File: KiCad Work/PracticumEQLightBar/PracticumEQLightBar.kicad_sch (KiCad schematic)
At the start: 2 parts, among them U1 TEENSY 4.1, U2 TEENSY AUDIO ADAPTER BOARD RE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

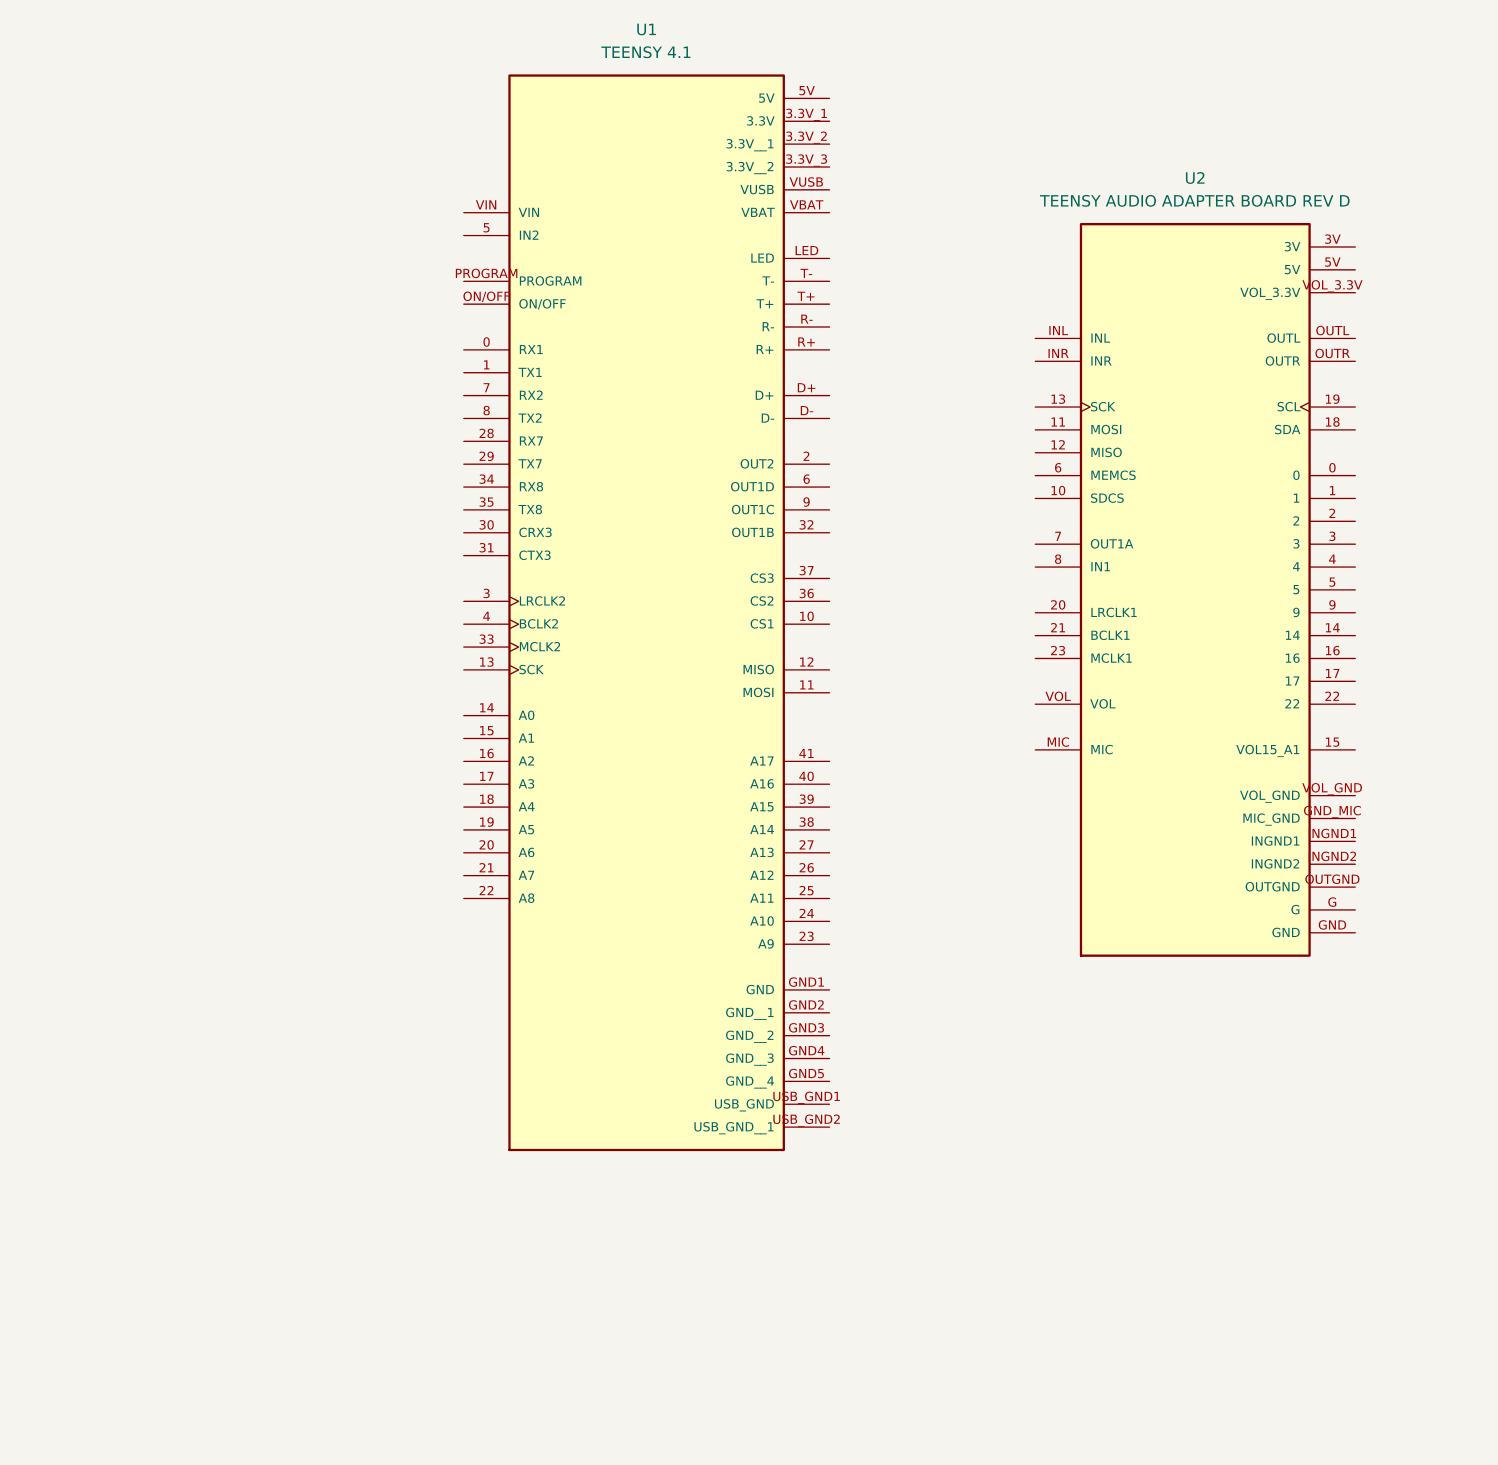
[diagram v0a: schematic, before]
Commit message: Added LEDs and wired them in schematic
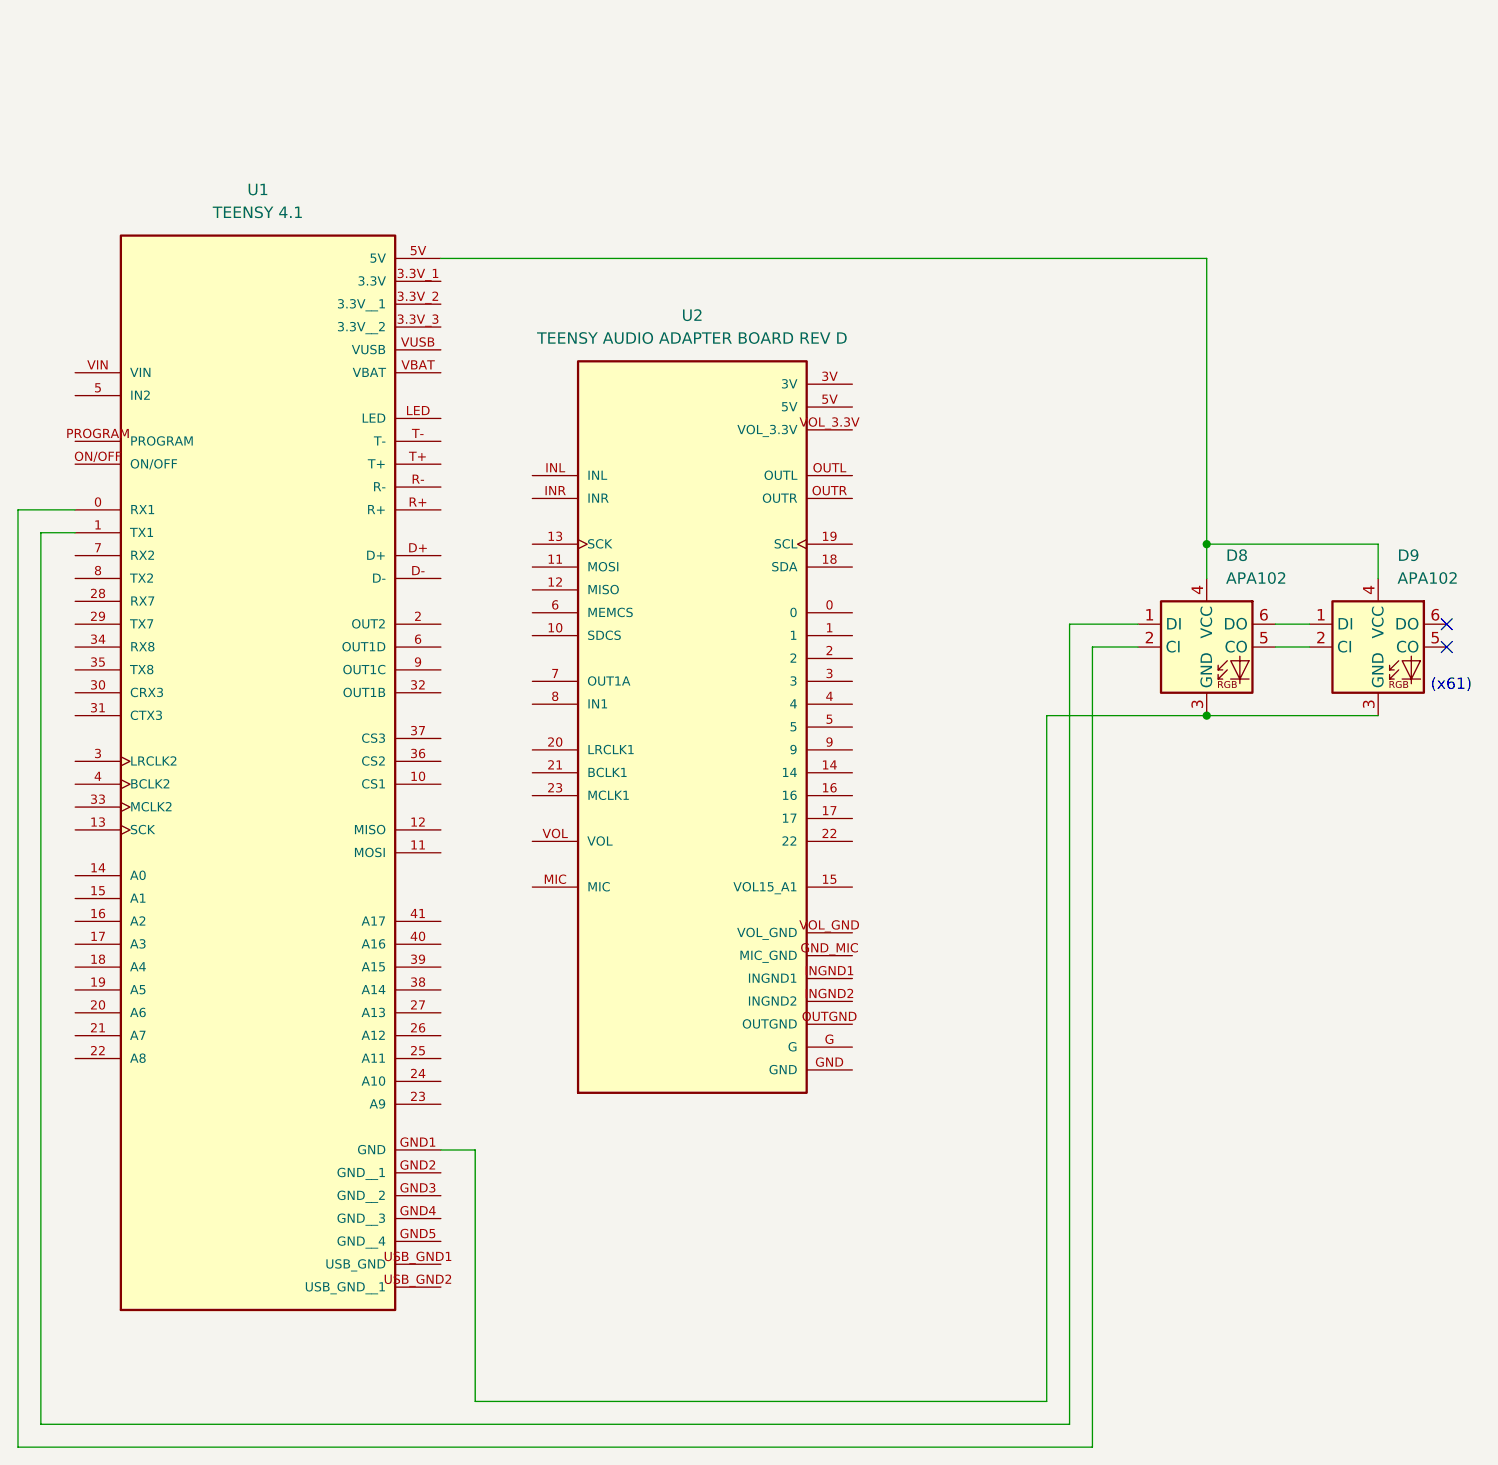
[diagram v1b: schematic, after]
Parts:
- added D8, D9: APA102, LED_SMD:LED_RGB_5050-6, symbol LED:APA102
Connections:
- net at U1.0 (RX1): now also D8.2 (CI)
- net at U1.1 (TX1): now also D8.1 (DI)
- net at U1.5V: now also D8.4 (VCC), D9.4 (VCC)
- net at U1.GND1 (GND): now also D8.3 (GND), D9.3 (GND)
- new net: D8.5 (CO), D9.2 (CI)
- new net: D8.6 (DO), D9.1 (DI)
- no-connect marks 0 -> 2
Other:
- note added: "(x61)"
- moved on the sheet: U1, U2

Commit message: Updates to LED layout to match 49 key on schematic and PCB
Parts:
- added D1, D10, D11, D12, D13, D14, D15, D16, D17, D18, D19, D2, D20, D21, D22, D23, D24, D25, D26, D27, D28, D29, D3, D30, D31, D32, D33, D34, D35, D36, D37, D38, D39, D4, D40, D41, D42, D43, D44, D45, D46, D47, D48, D49, D5, D6, D7: APA102, LED_SMD:LED_RGB_5050-6, symbol LED:APA102
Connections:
- net at U1.0 (RX1): now also D1.2 (CI); no longer D8.2 (CI)
- net at U1.1 (TX1): now also D1.1 (DI); no longer D8.1 (DI)
- net at D8.4 (VCC), D9.4 (VCC), U1.5V: now also D1.4 (VCC), D10.4 (VCC), D11.4 (VCC), D12.4 (VCC), D13.4 (VCC), D14.4 (VCC), D15.4 (VCC), D16.4 (VCC), D17.4 (VCC), D18.4 (VCC), D19.4 (VCC), D2.4 (VCC), D20.4 (VCC), D21.4 (VCC), D22.4 (VCC), D23.4 (VCC), D24.4 (VCC), D25.4 (VCC), D26.4 (VCC), D27.4 (VCC), D28.4 (VCC), D29.4 (VCC), D3.4 (VCC), D30.4 (VCC), D31.4 (VCC), D32.4 (VCC), D33.4 (VCC), D34.4 (VCC), D35.4 (VCC), D36.4 (VCC), D37.4 (VCC), D38.4 (VCC), D39.4 (VCC), D4.4 (VCC), D40.4 (VCC), D41.4 (VCC), D42.4 (VCC), D43.4 (VCC), D44.4 (VCC), D45.4 (VCC), D46.4 (VCC), D47.4 (VCC), D48.4 (VCC), D49.4 (VCC), D5.4 (VCC), D6.4 (VCC), D7.4 (VCC)
- net GND: now reaches D8.3 (GND), D9.3 (GND)
- net GND: now also D1.3 (GND), D10.3 (GND), D11.3 (GND), D12.3 (GND), D13.3 (GND), D14.3 (GND), D15.3 (GND), D16.3 (GND), D17.3 (GND), D18.3 (GND), D19.3 (GND), D2.3 (GND), D20.3 (GND), D21.3 (GND), D22.3 (GND), D23.3 (GND), D24.3 (GND), D25.3 (GND), D26.3 (GND), D27.3 (GND), D28.3 (GND), D29.3 (GND), D3.3 (GND), D30.3 (GND), D31.3 (GND), D32.3 (GND), D33.3 (GND), D34.3 (GND), D35.3 (GND), D36.3 (GND), D37.3 (GND), D38.3 (GND), D39.3 (GND), D4.3 (GND), D40.3 (GND), D41.3 (GND), D42.3 (GND), D43.3 (GND), D44.3 (GND), D45.3 (GND), D46.3 (GND), D47.3 (GND), D48.3 (GND), D49.3 (GND), D5.3 (GND), D6.3 (GND), D7.3 (GND); no longer U1.GND1 (GND)
- net at D9.5 (CO): now also D10.2 (CI)
- net at D9.6 (DO): now also D10.1 (DI)
- new net: D18.6 (DO), D19.1 (DI)
- new net: D18.5 (CO), D19.2 (CI)
- new net: D19.5 (CO), D20.2 (CI)
- new net: D19.6 (DO), D20.1 (DI)
- new net: D36.6 (DO), D37.1 (DI)
- new net: D36.5 (CO), D37.2 (CI)
- new net: D37.5 (CO), D38.2 (CI)
- new net: D37.6 (DO), D38.1 (DI)
- new net: D30.6 (DO), D31.1 (DI)
- new net: D30.5 (CO), D31.2 (CI)
- new net: D31.5 (CO), D32.2 (CI)
- new net: D31.6 (DO), D32.1 (DI)
- new net: D1.6 (DO), D2.1 (DI)
- new net: D1.5 (CO), D2.2 (CI)
- new net: D2.5 (CO), D3.2 (CI)
- new net: D2.6 (DO), D3.1 (DI)
- new net: D41.6 (DO), D42.1 (DI)
- new net: D41.5 (CO), D42.2 (CI)
- new net: D42.5 (CO), D43.2 (CI)
- new net: D42.6 (DO), D43.1 (DI)
- new net: D39.6 (DO), D40.1 (DI)
- new net: D39.5 (CO), D40.2 (CI)
- new net: D40.5 (CO), D41.2 (CI)
- new net: D40.6 (DO), D41.1 (DI)
- new net: D20.5 (CO), D21.2 (CI)
- new net: D20.6 (DO), D21.1 (DI)
- new net: D16.6 (DO), D17.1 (DI)
- new net: D16.5 (CO), D17.2 (CI)
- new net: D17.5 (CO), D18.2 (CI)
- new net: D17.6 (DO), D18.1 (DI)
- new net: D27.6 (DO), D28.1 (DI)
- new net: D27.5 (CO), D28.2 (CI)
- new net: D28.5 (CO), D29.2 (CI)
- new net: D28.6 (DO), D29.1 (DI)
- new net: D21.5 (CO), D22.2 (CI)
- new net: D21.6 (DO), D22.1 (DI)
- new net: D3.6 (DO), D4.1 (DI)
- new net: D3.5 (CO), D4.2 (CI)
- new net: D4.5 (CO), D5.2 (CI)
- new net: D4.6 (DO), D5.1 (DI)
- new net: D29.6 (DO), D30.1 (DI)
- new net: D29.5 (CO), D30.2 (CI)
- new net: D22.5 (CO), D23.2 (CI)
- new net: D22.6 (DO), D23.1 (DI)
- new net: D38.5 (CO), D39.2 (CI)
- new net: D38.6 (DO), D39.1 (DI)
- new net: D10.5 (CO), D11.2 (CI)
- new net: D10.6 (DO), D11.1 (DI)
- new net: D45.6 (DO), D46.1 (DI)
- new net: D45.5 (CO), D46.2 (CI)
- new net: D46.5 (CO), D47.2 (CI)
- new net: D46.6 (DO), D47.1 (DI)
- new net: D32.6 (DO), D33.1 (DI)
- new net: D32.5 (CO), D33.2 (CI)
- new net: D33.5 (CO), D34.2 (CI)
- new net: D33.6 (DO), D34.1 (DI)
- new net: D7.6 (DO), D8.1 (DI)
- new net: D7.5 (CO), D8.2 (CI)
- new net: D13.6 (DO), D14.1 (DI)
- new net: D13.5 (CO), D14.2 (CI)
- new net: D14.5 (CO), D15.2 (CI)
- new net: D14.6 (DO), D15.1 (DI)
- new net: D23.5 (CO), D24.2 (CI)
- new net: D23.6 (DO), D24.1 (DI)
- new net: D47.5 (CO), D48.2 (CI)
- new net: D47.6 (DO), D48.1 (DI)
- new net: D43.6 (DO), D44.1 (DI)
- new net: D43.5 (CO), D44.2 (CI)
- new net: D44.5 (CO), D45.2 (CI)
- new net: D44.6 (DO), D45.1 (DI)
- new net: D12.6 (DO), D13.1 (DI)
- new net: D12.5 (CO), D13.2 (CI)
- new net: D15.5 (CO), D16.2 (CI)
- new net: D15.6 (DO), D16.1 (DI)
- new net: D11.6 (DO), D12.1 (DI)
- new net: D11.5 (CO), D12.2 (CI)
- new net: D48.6 (DO), D49.1 (DI)
- new net: D48.5 (CO), D49.2 (CI)
- new net: D24.6 (DO), D25.1 (DI)
- new net: D24.5 (CO), D25.2 (CI)
- new net: D25.5 (CO), D26.2 (CI)
- new net: D25.6 (DO), D26.1 (DI)
- new net: D35.6 (DO), D36.1 (DI)
- new net: D35.5 (CO), D36.2 (CI)
- new net: D26.5 (CO), D27.2 (CI)
- new net: D26.6 (DO), D27.1 (DI)
- new net: D5.5 (CO), D6.2 (CI)
- new net: D5.6 (DO), D6.1 (DI)
- new net: D6.5 (CO), D7.2 (CI)
- new net: D6.6 (DO), D7.1 (DI)
- new net: D34.6 (DO), D35.1 (DI)
- new net: D34.5 (CO), D35.2 (CI)
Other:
- note removed: "(x61)"
- moved on the sheet: D8

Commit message: Completed preliminary schematic
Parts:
- removed D10, D11, D12, D13, D14, D15, D16, D17, D18, D19, D20, D21, D22, D23, D24, D25, D26, D27, D28, D29, D30, D31, D32, D33, D34, D35, D36, D37, D38, D39, D40, D41, D42, D43, D8, D9: APA102, LED_SMD:LED_RGB_5050-6, symbol LED:APA102
- added J1: AudioJack3Pin, symbol Connector_Audio:AudioJack3
- added MK1: Microphone, symbol Device:Microphone
- added RV1: Volume Pot, symbol Device:R_Potentiometer_Small
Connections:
- net 5V USB: now reaches D1.4 (VCC), D2.4 (VCC), D3.4 (VCC), D4.4 (VCC), D44.4 (VCC), D45.4 (VCC), D46.4 (VCC), D47.4 (VCC), D48.4 (VCC), D49.4 (VCC), D5.4 (VCC), D6.4 (VCC), D7.4 (VCC)
- net 5V USB: now also U1.VIN, U2.5V; no longer U1.5V
- net at U1.0 (RX1): now also U2.0; no longer D1.2 (CI)
- net at U1.1 (TX1): now also U2.1; no longer D1.1 (DI)
- net at U1.10 (CS1): now also U2.10 (SDCS)
- net at U1.11 (MOSI): now also U2.11 (MOSI)
- net at U1.12 (MISO): now also U2.12 (MISO)
- net at U1.13 (SCK): now also U2.13 (SCK)
- net at U1.14 (A0): now also U2.14
- net at U1.15 (A1): now also U2.15 (VOL15_A1)
- net at U1.16 (A2): now also U2.16
- net at U1.17 (A3): now also U2.17
- net at U1.18 (A4): now also U2.18 (SDA)
- net at U1.19 (A5): now also U2.19 (SCL)
- net at U1.2 (OUT2): now also U2.2
- net at U1.20 (A6): now also U2.20 (LRCLK1)
- net at U1.21 (A7): now also U2.21 (BCLK1)
- net at U1.22 (A8): now also U2.22
- net at U1.23 (A9): now also U2.23 (MCLK1)
- net at U1.24 (A10): now also D1.2 (CI)
- net at U1.25 (A11): now also D1.1 (DI)
- net at U1.3 (LRCLK2): now also U2.3
- net at U1.3.3V_2 (3.3V__1): now also U2.3V
- net at U1.4 (BCLK2): now also U2.4
- net at U1.5 (IN2): now also U2.5
- net at U1.6 (OUT1D): now also U2.6 (MEMCS)
- net at U1.7 (RX2): now also U2.7 (OUT1A)
- net at U1.8 (TX2): now also U2.8 (IN1)
- net at U1.9 (OUT1C): now also U2.9
- net at U1.GND1 (GND): now also U2.GND
- net at U1.GND3 (GND__2): now also U2.G
- net at D7.6 (DO): now also D44.1 (DI)
- net at D7.5 (CO): now also D44.2 (CI)
- net at U2.GND_MIC (MIC_GND): now also MK1.1 (-)
- net at U2.INGND1: now also U2.INGND2, J1.S
- net at U2.INL: now also J1.T
- net at U2.INR: now also J1.R
- net at U2.MIC: now also MK1.2 (+)
- net at U2.VOL: now also RV1.2
- net at U2.VOL_3.3V: now also RV1.1
- net at U2.VOL_GND: now also RV1.3
- no-connect marks 2 -> 40
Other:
- note added: "! Audio I/O pins may need to be jumped onto PCB, if not jumped directly to user I/O panel !"
- note added: "! May need logic-level shifter (3V to 5V) to drive RGB LEDs with this board !"
- note added: "Powered via USB Micro-B port on Teensy 4.1 board"
- note added: "Repeated x5 to emulate 5 octaves of a 49 key piano"
- note added: "Shield connected via stacking headers"
- company: (none) -> Team 3, ECE 411, Fall 2025, Portland State University
- title: (none) -> Practicum Piano Light Bar, Preliminary
- moved on the sheet: D1, D2, D3, D4, D45, D46, D47, D48, D49, D5, D6, D7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

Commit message: Schematic and PCB updated to show all 49 LEDs
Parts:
- added D10, D11, D12, D13, D14, D15, D16, D17, D18, D19, D20, D21, D22, D23, D24, D25, D26, D27, D28, D29, D30, D31, D32, D33, D34, D35, D36, D37, D38, D39, D40, D41, D42, D43, D8, D9: APA102, LED_SMD:LED_RGB_5050-6, symbol LED:APA102
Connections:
- net 5V USB: now also D10.4 (VCC), D11.4 (VCC), D12.4 (VCC), D13.4 (VCC), D14.4 (VCC), D15.4 (VCC), D16.4 (VCC), D17.4 (VCC), D18.4 (VCC), D19.4 (VCC), D20.4 (VCC), D21.4 (VCC), D22.4 (VCC), D23.4 (VCC), D24.4 (VCC), D25.4 (VCC), D26.4 (VCC), D27.4 (VCC), D28.4 (VCC), D29.4 (VCC), D30.4 (VCC), D31.4 (VCC), D32.4 (VCC), D33.4 (VCC), D34.4 (VCC), D35.4 (VCC), D36.4 (VCC), D37.4 (VCC), D38.4 (VCC), D39.4 (VCC), D40.4 (VCC), D41.4 (VCC), D42.4 (VCC), D43.4 (VCC), D8.4 (VCC), D9.4 (VCC)
- net GND: now also D10.3 (GND), D11.3 (GND), D12.3 (GND), D13.3 (GND), D14.3 (GND), D15.3 (GND), D16.3 (GND), D17.3 (GND), D18.3 (GND), D19.3 (GND), D20.3 (GND), D21.3 (GND), D22.3 (GND), D23.3 (GND), D24.3 (GND), D25.3 (GND), D26.3 (GND), D27.3 (GND), D28.3 (GND), D29.3 (GND), D30.3 (GND), D31.3 (GND), D32.3 (GND), D33.3 (GND), D34.3 (GND), D35.3 (GND), D36.3 (GND), D37.3 (GND), D38.3 (GND), D39.3 (GND), D40.3 (GND), D41.3 (GND), D42.3 (GND), D43.3 (GND), D8.3 (GND), D9.3 (GND)
- net at D7.6 (DO): now also D8.1 (DI); no longer D44.1 (DI)
- net at D7.5 (CO): now also D8.2 (CI); no longer D44.2 (CI)
- new net: D10.1 (DI), D9.6 (DO)
- new net: D10.2 (CI), D9.5 (CO)
- new net: D10.5 (CO), D11.2 (CI)
- new net: D10.6 (DO), D11.1 (DI)
- new net: D15.6 (DO), D16.1 (DI)
- new net: D15.5 (CO), D16.2 (CI)
- new net: D16.5 (CO), D17.2 (CI)
- new net: D16.6 (DO), D17.1 (DI)
- new net: D20.6 (DO), D21.1 (DI)
- new net: D20.5 (CO), D21.2 (CI)
- new net: D21.5 (CO), D22.2 (CI)
- new net: D21.6 (DO), D22.1 (DI)
- new net: D14.6 (DO), D15.1 (DI)
- new net: D14.5 (CO), D15.2 (CI)
- new net: D12.6 (DO), D13.1 (DI)
- new net: D12.5 (CO), D13.2 (CI)
- new net: D13.5 (CO), D14.2 (CI)
- new net: D13.6 (DO), D14.1 (DI)
- new net: D25.6 (DO), D26.1 (DI)
- new net: D25.5 (CO), D26.2 (CI)
- new net: D26.5 (CO), D27.2 (CI)
- new net: D26.6 (DO), D27.1 (DI)
- new net: D29.6 (DO), D30.1 (DI)
- new net: D29.5 (CO), D30.2 (CI)
- new net: D30.5 (CO), D31.2 (CI)
- new net: D30.6 (DO), D31.1 (DI)
- new net: D27.5 (CO), D28.2 (CI)
- new net: D27.6 (DO), D28.1 (DI)
- new net: D41.6 (DO), D42.1 (DI)
- new net: D41.5 (CO), D42.2 (CI)
- new net: D42.5 (CO), D43.2 (CI)
- new net: D42.6 (DO), D43.1 (DI)
- new net: D17.6 (DO), D18.1 (DI)
- new net: D17.5 (CO), D18.2 (CI)
- new net: D18.5 (CO), D19.2 (CI)
- new net: D18.6 (DO), D19.1 (DI)
- new net: D19.6 (DO), D20.1 (DI)
- new net: D19.5 (CO), D20.2 (CI)
- new net: D8.5 (CO), D9.2 (CI)
- new net: D8.6 (DO), D9.1 (DI)
- new net: D37.6 (DO), D38.1 (DI)
- new net: D37.5 (CO), D38.2 (CI)
- new net: D38.5 (CO), D39.2 (CI)
- new net: D38.6 (DO), D39.1 (DI)
- new net: D22.5 (CO), D23.2 (CI)
- new net: D22.6 (DO), D23.1 (DI)
- new net: D23.6 (DO), D24.1 (DI)
- new net: D23.5 (CO), D24.2 (CI)
- new net: D24.5 (CO), D25.2 (CI)
- new net: D24.6 (DO), D25.1 (DI)
- new net: D43.5 (CO), D44.2 (CI)
- new net: D43.6 (DO), D44.1 (DI)
- new net: D36.6 (DO), D37.1 (DI)
- new net: D36.5 (CO), D37.2 (CI)
- new net: D33.6 (DO), D34.1 (DI)
- new net: D33.5 (CO), D34.2 (CI)
- new net: D34.5 (CO), D35.2 (CI)
- new net: D34.6 (DO), D35.1 (DI)
- new net: D31.5 (CO), D32.2 (CI)
- new net: D31.6 (DO), D32.1 (DI)
- new net: D32.6 (DO), D33.1 (DI)
- new net: D32.5 (CO), D33.2 (CI)
- new net: D28.6 (DO), D29.1 (DI)
- new net: D28.5 (CO), D29.2 (CI)
- new net: D40.6 (DO), D41.1 (DI)
- new net: D40.5 (CO), D41.2 (CI)
- new net: D35.6 (DO), D36.1 (DI)
- new net: D35.5 (CO), D36.2 (CI)
- new net: D39.6 (DO), D40.1 (DI)
- new net: D39.5 (CO), D40.2 (CI)
- new net: D11.6 (DO), D12.1 (DI)
- new net: D11.5 (CO), D12.2 (CI)
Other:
- note removed: "Repeated x5 to emulate 5 octaves of a 49 key piano"
- moved on the sheet: D1, D2, D3, D4, D45, D46, D47, D48, D49, D5, D6, D7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

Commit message: Resized edge cuts and updated titleblocks
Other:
- title: Practicum Piano Light Bar, Preliminary -> EchoKeys 49
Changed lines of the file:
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@@
 	(paper "A2")
 	(title_block
-		(title "Practicum Piano Light Bar, Preliminary")
-		(date "2025-10-30")
+		(title "EchoKeys 49")
+		(date "2025-11-08")
 		(rev "1")
 		(company "Team 3, ECE 411, Fall 2025, Portland State University")
